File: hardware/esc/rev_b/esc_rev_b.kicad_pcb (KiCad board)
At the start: 6 copper layers, 150 x 150 mm, 646 parts, among them J1101 FUSED_BATTERY_TAP, J1102 MOTOR_PHASES, J1103 LOCAL_SWD, J1201 FUSED_BATTERY_TAP, J1202 MOTOR_PHASES, J1203 LOCAL_SWD, J1301 FUSED_BATTERY_TAP, J1302 MOTOR_PHASES, J1303 LOCAL_SWD, J1401 FUSED_BATTERY_TAP, J1402 MOTOR_PHASES, J1403 LOCAL_SWD, J1501 FUSED_BATTERY_TAP, J1502 MOTOR_PHASES, J1503 LOCAL_SWD, J1601 FUSED_BATTERY_TAP, J1602 MOTOR_PHASES, J1603 LOCAL_SWD, J201 ESC_SWD, J701 AUX_BATTERY, J702 FLIGHT_CAN_POWER, Q1101 IPTC014N10NM5, Q1102 IPTC014N10NM5, Q1103 IPTC014N10NM5, Q1104 IPTC014N10NM5, Q1105 IPTC014N10NM5, Q1106 IPTC014N10NM5, Q1201 IPTC014N10NM5, Q1202 IPTC014N10NM5, Q1203 IPTC014N10NM5, Q1204 IPTC014N10NM5, Q1205 IPTC014N10NM5, Q1206 IPTC014N10NM5, Q1301 IPTC014N10NM5, Q1302 IPTC014N10NM5, Q1303 IPTC014N10NM5, Q1304 IPTC014N10NM5, Q1305 IPTC014N10NM5, Q1306 IPTC014N10NM5, Q1401 IPTC014N10NM5, Q1402 IPTC014N10NM5, Q1403 IPTC014N10NM5, Q1404 IPTC014N10NM5, Q1405 IPTC014N10NM5, Q1406 IPTC014N10NM5, Q1501 IPTC014N10NM5, Q1502 IPTC014N10NM5, Q1503 IPTC014N10NM5, Q1504 IPTC014N10NM5, Q1505 IPTC014N10NM5, Q1506 IPTC014N10NM5, Q1601 IPTC014N10NM5, Q1602 IPTC014N10NM5, Q1603 IPTC014N10NM5, Q1604 IPTC014N10NM5, Q1605 IPTC014N10NM5, Q1606 IPTC014N10NM5, U1101 DRV8353SRTAR, U1102 STM32G431CBT6, U1103 ISO6731FDWR, U1104 TPS70933DBVR, U1105 INA296A2IDR, U1106 SN74LVC1G08DBVR, U1201 DRV8353SRTAR, U1202 STM32G431CBT6, U1203 ISO6731FDWR, U1204 TPS70933DBVR, U1205 INA296A2IDR, U1206 SN74LVC1G08DBVR, U1301 DRV8353SRTAR, U1302 STM32G431CBT6, U1303 ISO6731FDWR, U1304 TPS70933DBVR, U1305 INA296A2IDR, U1306 SN74LVC1G08DBVR, U1401 DRV8353SRTAR, U1402 STM32G431CBT6, U1403 ISO6731FDWR, U1404 TPS70933DBVR, U1405 INA296A2IDR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

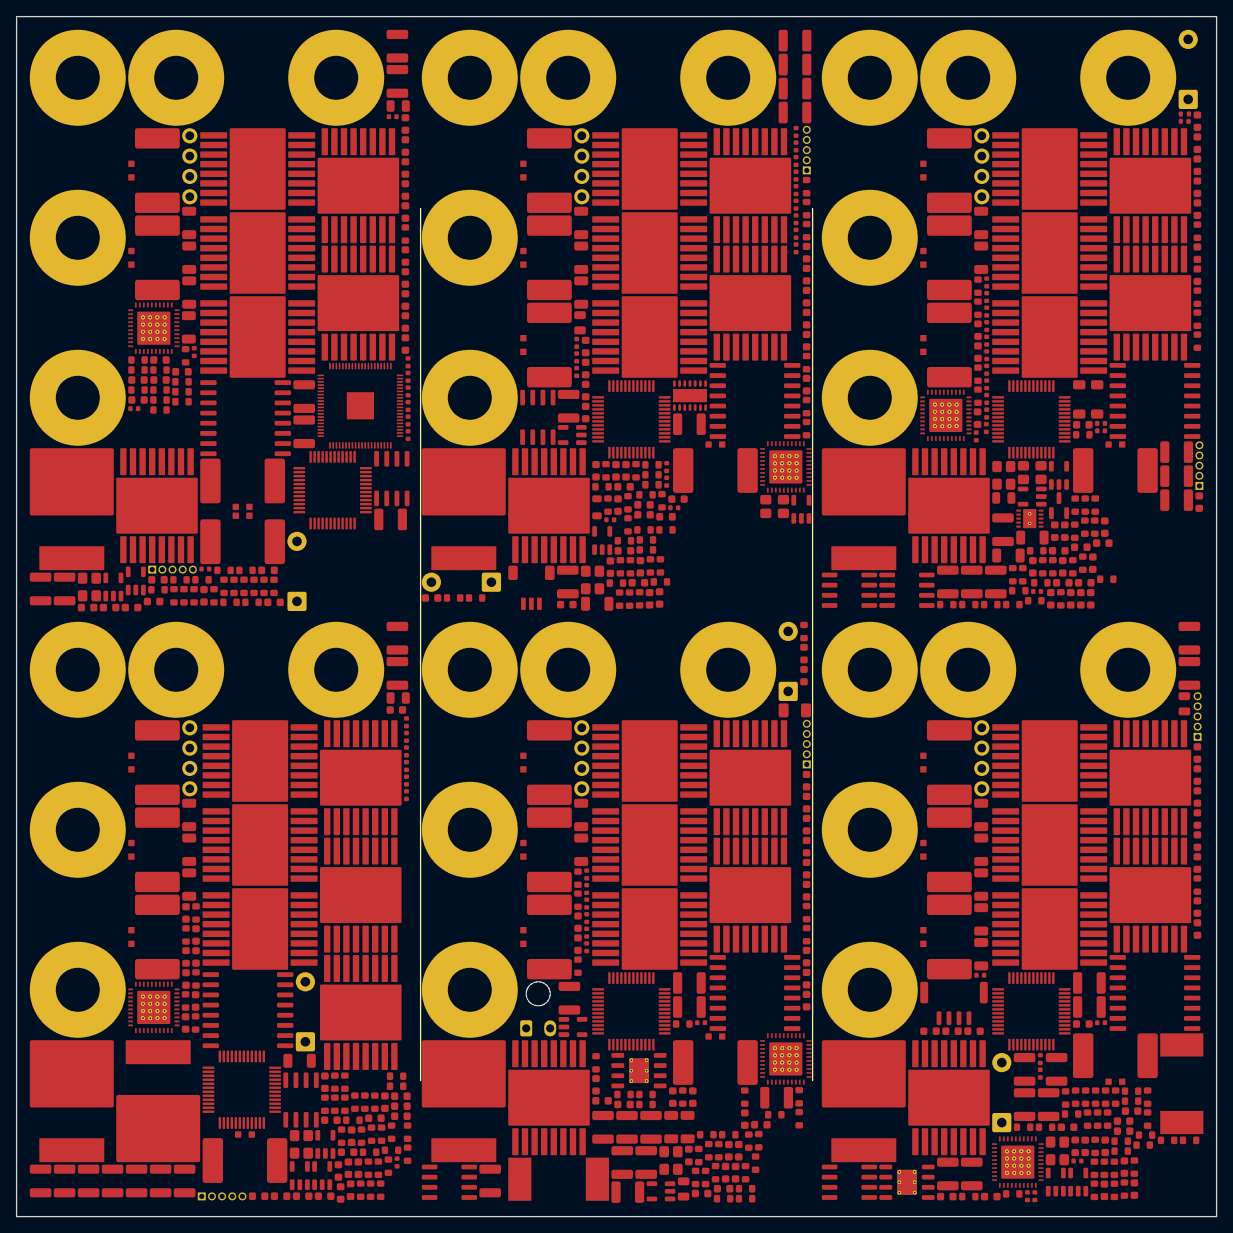
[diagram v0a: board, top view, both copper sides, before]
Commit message: esc: repack components without physical collisions
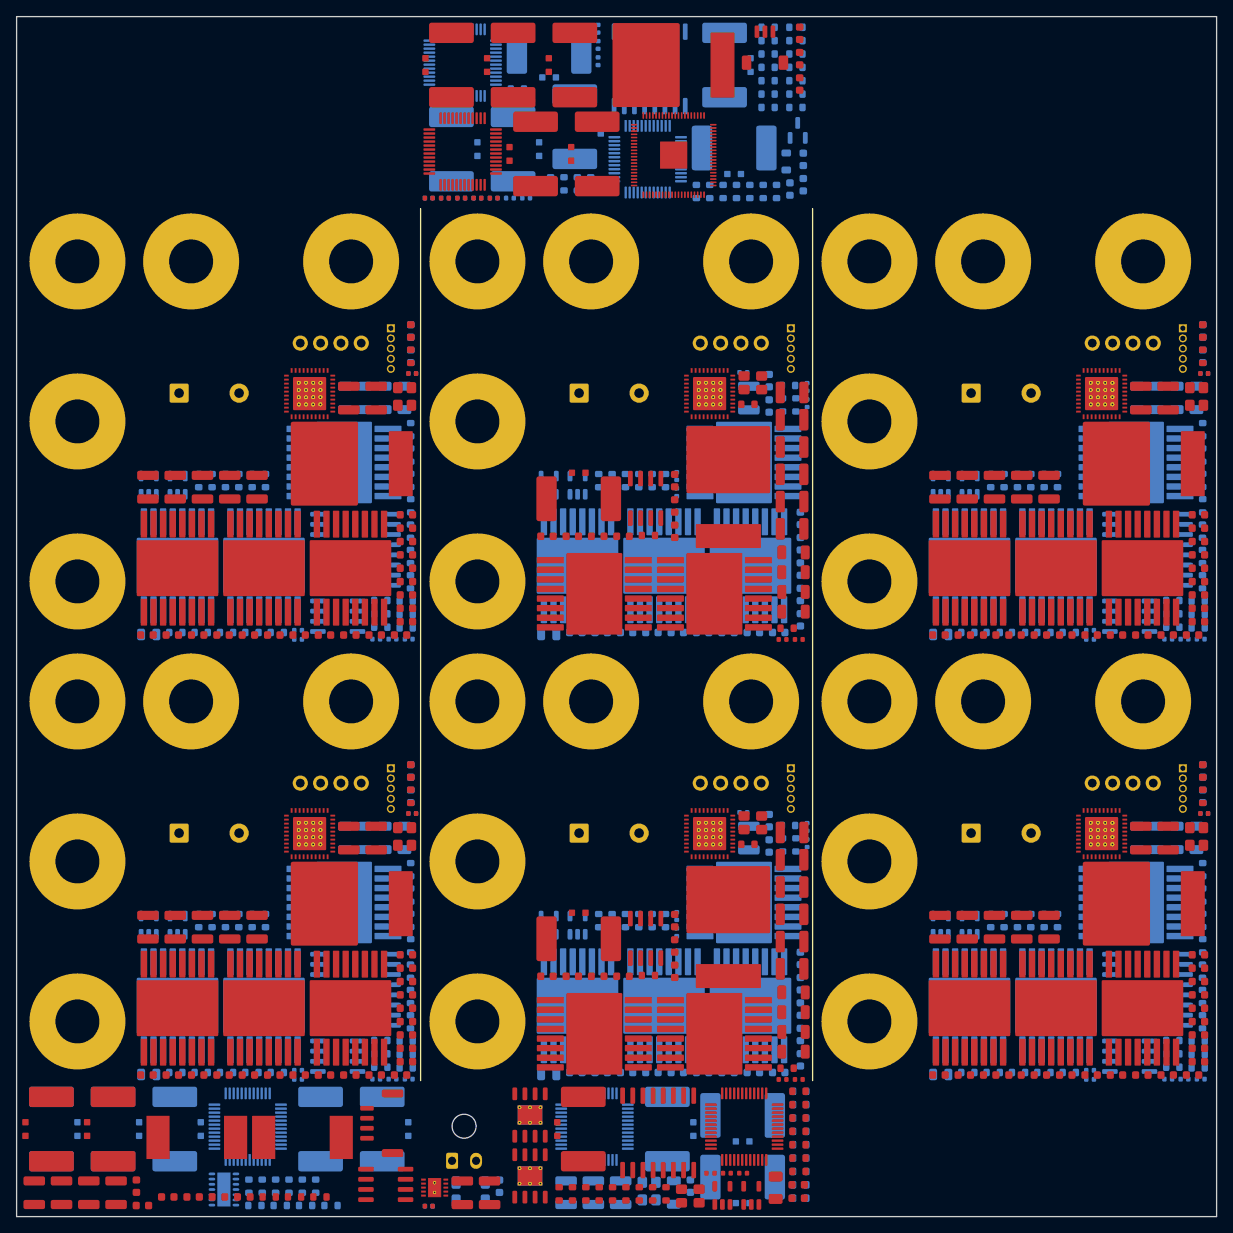
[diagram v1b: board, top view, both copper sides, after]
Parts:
- C1160, C1167, C1169, C1170, C1172, C1173, C1174, C1177, C1201, C1202, C1207, C1220, C1221, C1222, C1223, C1236, C1250, C1260, C1261, C1262, C1263, C1264, C1265, C1266, C1269, C1270, C1271, C1272, C1273, C1274, C1275, C1360, C1367, C1369, C1370, C1372, C1373, C1374, C1377, C1460, C1467, C1469, C1470, C1472, C1473, C1474, C1477, C1501, C1502, C1507, C1520, C1521, C1522, C1523, C1536, C1550, C1560, C1561, C1562, C1563, C1564, C1565, C1566, C1569, C1570, C1571, C1572, C1573, C1574, C1575, C1660, C1667, C1669, C1670, C1672, C1673, C1674, C1677, C201, C202, C205, C212, C213, C214, C215, C216, C217, C218, C219, C232, C233, C240, C241, C703, C706, C707, C711, C713, C714, D1102, D1302, D1402, D1602, D202, FL201, L201, Q1104, Q1105, Q1106, Q1203, Q1204, Q1205, Q1206, Q1304, Q1305, Q1306, Q1404, Q1405, Q1406, Q1503, Q1504, Q1505, Q1506, Q1604, Q1605, Q1606, R1102, R1103, R1104, R1105, R1106, R1107, R1108, R1109, R1110, R1111, R1112, R1120, R1121, R1122, R1123, R1130, R1131, R1132, R1133, R1140, R1141, R1142, R1143, R1144, R1145, R1150, R1151, R1152, R1153, R1154, R1155, R1156, R1157, R1158, R1159, R1204, R1205, R1206, R1207, R1208, R1209, R1210, R1211, R1212, R1221, R1222, R1230, R1231, R1232, R1233, R1244, R1245, R1250, R1251, R1252, R1253, R1254, R1255, R1256, R1257, R1258, R1259, R1302, R1303, R1304, R1305, R1306, R1307, R1308, R1309, R1310, R1311, R1312, R1330, R1331, R1332, R1333, R1340, R1341, R1342, R1343, R1344, R1345, R1350, R1351, R1352, R1353, R1354, R1355, R1356, R1357, R1358, R1359, R1402, R1403, R1404, R1405, R1406, R1407, R1408, R1409, R1410, R1411, R1412, R1420, R1421, R1422, R1430, R1431, R1432, R1433, R1440, R1441, R1442, R1443, R1444, R1445, R1450, R1451, R1452, R1453, R1454, R1455, R1456, R1457, R1458, R1459, R1504, R1505, R1506, R1507, R1508, R1509, R1510, R1511, R1512, R1521, R1522, R1523, R1530, R1531, R1532, R1533, R1544, R1602, R1603, R1604, R1605, R1606, R1607, R1608, R1609, R1610, R1611, R1612, R1620, R1621, R1630, R1631, R1632, R1633, R1640, R1641, R1642, R1643, R1644, R1645, R1650, R1651, R1652, R1653, R1654, R1655, R1656, R240, R241, R242, R701, R702, R703, R704, R705, R710, R711, R712, R713, TH1, TH2, TH3, TH4, U1102, U1103, U1104, U1105, U1106, U1202, U1203, U1204, U1206, U1303, U1304, U1305, U1306, U1402, U1403, U1404, U1405, U1406, U1504, U1506, U1602, U1603, U1604, U1605, U1606, U207, Y202: moved to B.Cu
- moved C231 147.2 mm to (15.7, 148.6), turned to 0 degrees
- moved C708 145.6 mm to (97.9, 2.08), turned to 90 degrees
- moved R201 145.1 mm to (86.7, 144.6)
- moved D701 144.8 mm to (81.8, 6.05), turned to 90 degrees
- moved C709 136.8 mm to (97.9, 5.25)
- moved C706 135.2 mm to (98.3, 17.8)
- moved D201 133.6 mm to (25.2, 147.5), turned to 0 degrees
- moved C712 133.6 mm to (97.9, 8.43)
- moved C205 133.3 mm to (51.5, 148.7), turned to 0 degrees
- moved FB201 132.1 mm to (28.4, 147.5), turned to 0 degrees
- moved R202 130.6 mm to (31.6, 147.5), turned to 0 degrees
- moved C702 127.3 mm to (2.21, 147.0)
- moved C707 126.0 mm to (98.3, 21.0)
- moved R1623 125.6 mm to (12.1, 139.1), turned to 90 degrees
- moved FL201 125.6 mm to (56.8, 146.9), turned to 0 degrees
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
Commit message: revert ESC to front-side-only placement from 325f93b; main board CANL routing + ACT45B pinout fix
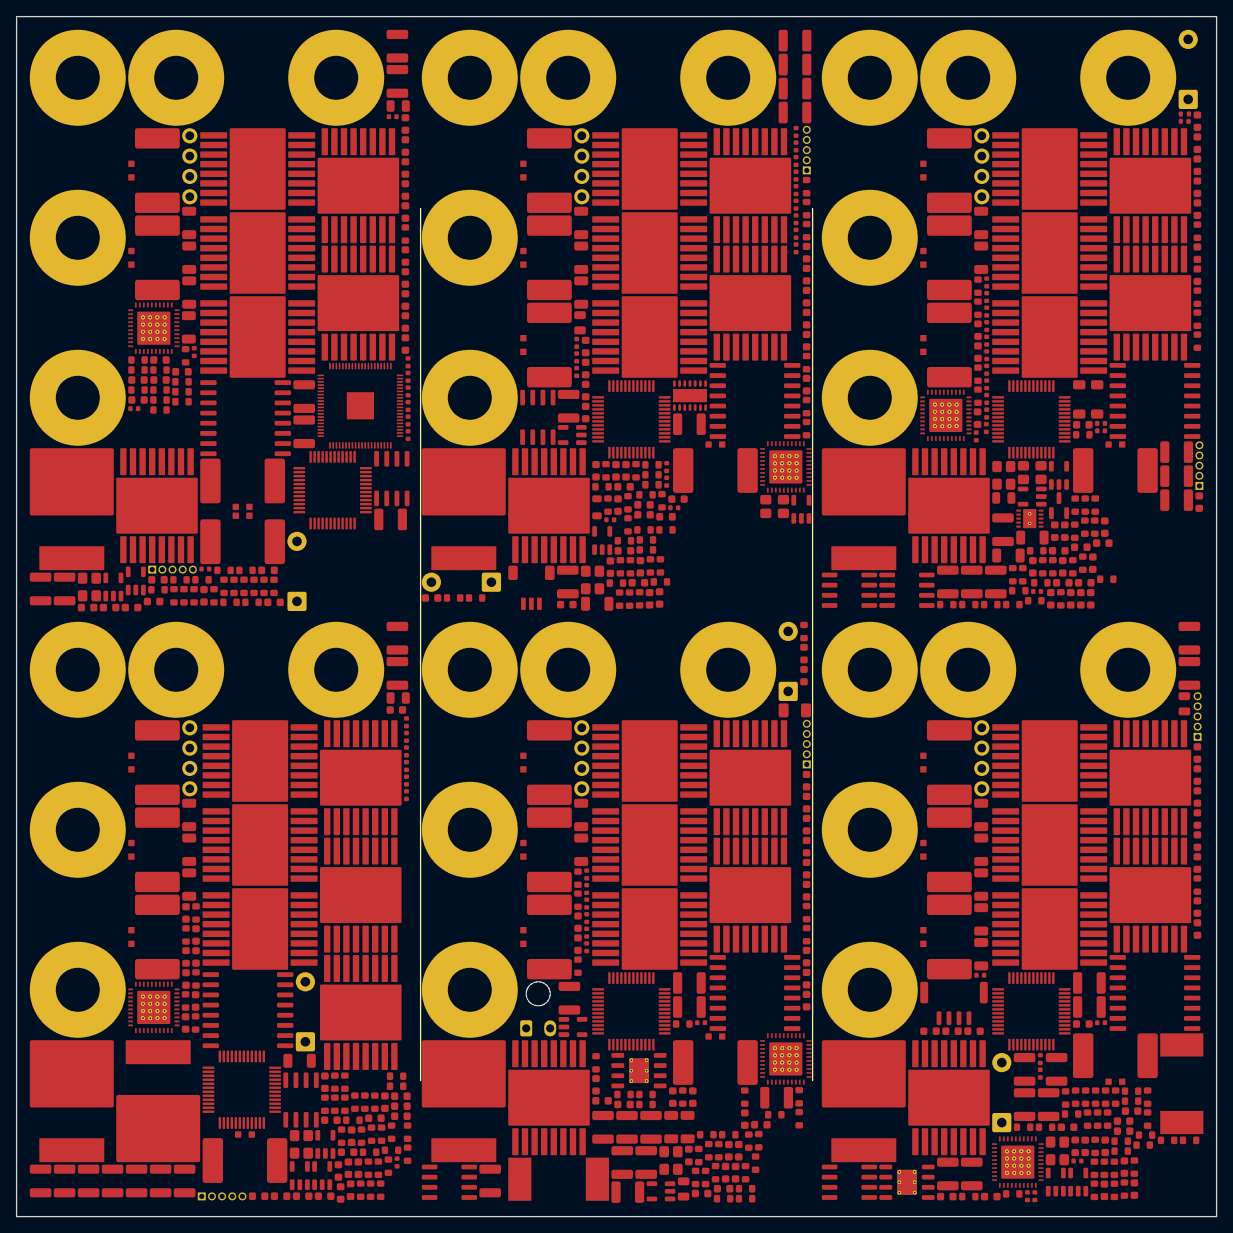
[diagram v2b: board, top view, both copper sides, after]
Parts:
- C1160, C1167, C1169, C1170, C1172, C1173, C1174, C1177, C1201, C1202, C1207, C1220, C1221, C1222, C1223, C1236, C1250, C1260, C1261, C1262, C1263, C1264, C1265, C1266, C1269, C1270, C1271, C1272, C1273, C1274, C1275, C1360, C1367, C1369, C1370, C1372, C1373, C1374, C1377, C1460, C1467, C1469, C1470, C1472, C1473, C1474, C1477, C1501, C1502, C1507, C1520, C1521, C1522, C1523, C1536, C1550, C1560, C1561, C1562, C1563, C1564, C1565, C1566, C1569, C1570, C1571, C1572, C1573, C1574, C1575, C1660, C1667, C1669, C1670, C1672, C1673, C1674, C1677, C201, C202, C205, C212, C213, C214, C215, C216, C217, C218, C219, C232, C233, C240, C241, C703, C706, C707, C711, C713, C714, D1102, D1302, D1402, D1602, D202, FL201, L201, Q1104, Q1105, Q1106, Q1203, Q1204, Q1205, Q1206, Q1304, Q1305, Q1306, Q1404, Q1405, Q1406, Q1503, Q1504, Q1505, Q1506, Q1604, Q1605, Q1606, R1102, R1103, R1104, R1105, R1106, R1107, R1108, R1109, R1110, R1111, R1112, R1120, R1121, R1122, R1123, R1130, R1131, R1132, R1133, R1140, R1141, R1142, R1143, R1144, R1145, R1150, R1151, R1152, R1153, R1154, R1155, R1156, R1157, R1158, R1159, R1204, R1205, R1206, R1207, R1208, R1209, R1210, R1211, R1212, R1221, R1222, R1230, R1231, R1232, R1233, R1244, R1245, R1250, R1251, R1252, R1253, R1254, R1255, R1256, R1257, R1258, R1259, R1302, R1303, R1304, R1305, R1306, R1307, R1308, R1309, R1310, R1311, R1312, R1330, R1331, R1332, R1333, R1340, R1341, R1342, R1343, R1344, R1345, R1350, R1351, R1352, R1353, R1354, R1355, R1356, R1357, R1358, R1359, R1402, R1403, R1404, R1405, R1406, R1407, R1408, R1409, R1410, R1411, R1412, R1420, R1421, R1422, R1430, R1431, R1432, R1433, R1440, R1441, R1442, R1443, R1444, R1445, R1450, R1451, R1452, R1453, R1454, R1455, R1456, R1457, R1458, R1459, R1504, R1505, R1506, R1507, R1508, R1509, R1510, R1511, R1512, R1521, R1522, R1523, R1530, R1531, R1532, R1533, R1544, R1602, R1603, R1604, R1605, R1606, R1607, R1608, R1609, R1610, R1611, R1612, R1620, R1621, R1630, R1631, R1632, R1633, R1640, R1641, R1642, R1643, R1644, R1645, R1650, R1651, R1652, R1653, R1654, R1655, R1656, R240, R241, R242, R701, R702, R703, R704, R705, R710, R711, R712, R713, TH1, TH2, TH3, TH4, U1102, U1103, U1104, U1105, U1106, U1202, U1203, U1204, U1206, U1303, U1304, U1305, U1306, U1402, U1403, U1404, U1405, U1406, U1504, U1506, U1602, U1603, U1604, U1605, U1606, U207, Y202: moved to F.Cu
- moved C231 147.2 mm to (136.0, 63.8), turned to 90 degrees
- moved C708 145.6 mm to (44.8, 137.7), turned to 180 degrees
- moved R201 145.1 mm to (146.0, 12.2)
- moved D701 144.8 mm to (17.7, 135.8), turned to 180 degrees
- moved C709 136.8 mm to (89.0, 141.8)
- moved C706 135.2 mm to (139.7, 146.6)
- moved D201 133.6 mm to (129.8, 64.3), turned to 90 degrees
- moved C712 133.6 mm to (90.3, 141.8)
- moved C205 133.3 mm to (97.4, 23.5), turned to 90 degrees
- moved FB201 132.1 mm to (131.0, 64.3), turned to 90 degrees
- moved R202 130.6 mm to (132.3, 64.3), turned to 90 degrees
- moved C702 127.3 mm to (129.0, 136.0)
- moved C707 126.0 mm to (46.0, 135.7)
- moved R1623 125.6 mm to (137.3, 129.9), turned to 180 degrees
- moved FL201 125.6 mm to (133.9, 47.9), turned to 90 degrees
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
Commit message: esc: restore physically valid all-front layout
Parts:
- moved J1301 214.9 mm to (12.0, 188.0), turned to 90 degrees
- moved PS1301 205.0 mm to (42.0, 208.0), turned to 0 degrees
- moved D1502 203.4 mm to (94.0, 283.0), turned to 0 degrees
- moved J1501 201.8 mm to (12.0, 272.0), turned to 90 degrees
- moved C1660 201.6 mm to (178.8, 284.9), turned to 0 degrees
- moved PS1501 201.3 mm to (42.0, 292.0), turned to 0 degrees
- moved C1330 200.8 mm to (13.0, 160.5), turned to 0 degrees
- moved PS1601 200.0 mm to (138.0, 292.0), turned to 0 degrees
- moved U1303 195.0 mm to (28.0, 206.0)
- moved C1504 194.8 mm to (45.4, 285.6)
- moved R1622 194.8 mm to (172.0, 280.0), turned to -90 degrees
- moved C1503 193.7 mm to (45.4, 281.8)
- moved C1571 193.2 mm to (93.3, 275.6)
- moved R1423 192.1 mm to (186.0, 207.4), turned to 0 degrees
- moved J1601 191.5 mm to (108.0, 272.0), turned to 90 degrees
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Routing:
- net /Motor 1 power cell/M1_SHC_N: track 0.00 -> 31.9 mm
- net /Motor 5 power cell/M5_SHC_N: track 0.00 -> 31.9 mm
- net /Motor 3 power cell/M3_SHC_N: track 0.00 -> 31.9 mm
- net /Motor 6 power cell/M6_SHC_N: track 0.00 -> 31.9 mm
- net /Motor 2 power cell/M2_SHC_N: track 0.00 -> 31.9 mm
- net /Motor 4 power cell/M4_SHC_N: track 0.00 -> 31.9 mm
- net /Motor 1 power cell/M1_SHC_P: track 0.00 -> 30.0 mm
- net /Motor 3 power cell/M3_SHC_P: track 0.00 -> 30.0 mm
- net /Motor 2 power cell/M2_SHC_P: track 0.00 -> 30.0 mm
- net /Motor 4 power cell/M4_SHC_P: track 0.00 -> 30.0 mm
- net /Motor 5 power cell/M5_SHC_P: track 0.00 -> 30.0 mm
- net /Motor 6 power cell/M6_SHC_P: track 0.00 -> 30.0 mm
- net /Motor 5 power cell/M5_SHA_N: track 0.00 -> 18.0 mm
- net /Motor 6 power cell/M6_SHA_N: track 0.00 -> 18.0 mm
- net /Motor 4 power cell/M4_SHA_N: track 0.00 -> 18.0 mm
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- added copper zone on B.Cu, net /DGND
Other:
- board size 150 x 150 mm -> 196 x 296 mm
- copper layers 6 -> 4
- board text added: "AUX POWER - TWO INDEPENDENT 1 A RAILS"
- board text added: "ESC SUPERVISOR / CAN FD"
- board text added: "MOTOR 1 - 60 A CELL"
- board text added: "MOTOR 2 - 60 A CELL"
- board text added: "MOTOR 3 - 60 A CELL"
- board text added: "MOTOR 4 - 60 A CELL"
- board text added: "MOTOR 5 - 60 A CELL"
- board text added: "MOTOR 6 - 60 A CELL"
- board text added: "REV-B | 4 oz OUTER / 1.5 oz INNER | 6 x 60 A"
- board text removed: "M1"
- board text removed: "M2"
- board text removed: "M3"
- board text removed: "M4"
- board text removed: "M5"
- board text removed: "M6"
- board text removed: "REV-B 150MM SIX-LAYER ESC PLACEMENT CANDIDATE"

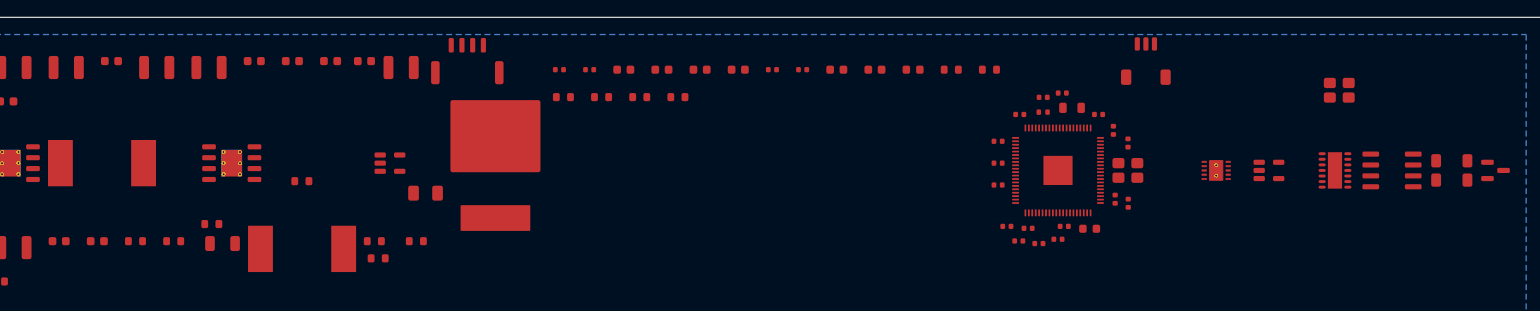
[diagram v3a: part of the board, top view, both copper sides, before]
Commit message: esc: hand route first ten signal links
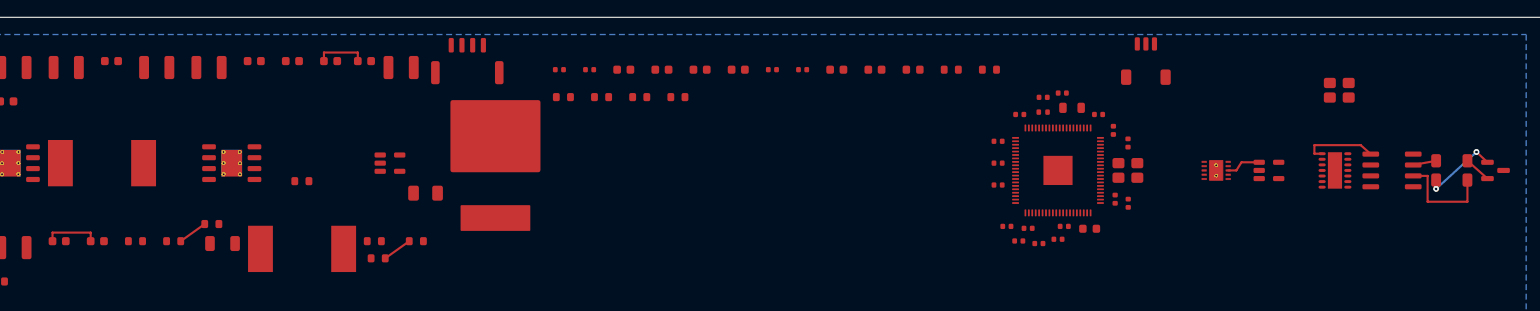
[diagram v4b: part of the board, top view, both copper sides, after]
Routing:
- net /Controller and ADC/U206_CANL: track 0.00 -> 11.9 mm
- net /CANH: track 0.00 -> 9.16 mm, vias 0 -> 2
- net /Controller and ADC/U207_TXCAN: track 0.00 -> 8.87 mm
- net /Auxiliary power/LM2_RIPPLE: track 0.00 -> 6.45 mm
- net /Auxiliary power/LM_RIPPLE: track 0.00 -> 5.95 mm
- net /Controller and ADC/ESC_RUN: track 0.00 -> 4.14 mm
- net /Auxiliary power/LM_FB: track 0.00 -> 3.44 mm
- net /Auxiliary power/LM2_FB: track 0.00 -> 3.44 mm
- net /CANL: track 0.00 -> 3.13 mm
- net /Controller and ADC/U206_CANH: track 0.00 -> 2.71 mm
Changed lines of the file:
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@@
 	)
 	(segment
+		(start 60.95 28.1)
+		(end 63.75 26.1)
+		(width 0.25)
+		(layer "F.Cu")
+		(net 9)
+	)
+	(segment
+		(start 22.15 25.1)
+		(end 26.6 25.1)
+		(width 0.25)
+		(layer "F.Cu")
+		(net 10)
+	)
+	(segment
+		(start 26.6 25.1)
+		(end 26.6 26.1)
+		(width 0.25)
+		(layer "F.Cu")
+		(net 10)
+	)
+	(segment
+		(start 22.15 26.1)
+		(end 22.15 25.1)
+		(width 0.25)
+		(layer "F.Cu")
+		(net 10)
+	)
+	(segment
+		(start 37.1 26.1)
+		(end 39.9 24.1)
+		(width 0.25)
+		(layer "F.Cu")
+		(net 14)
+	)
+	(segment
+		(start 53.8 4.099999)
+		(end 57.75 4.099999)
+		(width 0.25)
+		(layer "F.Cu")
+		(net 15)
+	)
+	(segment
+		(start 53.8 5.1)
+		(end 53.8 4.099999)
+		(width 0.25)
+		(layer "F.Cu")
+		(net 15)
+	)
+	(segment
+		(start 57.75 4.099999)
+		(end 57.75 5.1)
+		(width 0.25)
+		(layer "F.Cu")
+		(net 15)
+	)
+	(segment
+		(start 183.495 18.974999)
+		(end 183.495 20)
+		(width 0.25)
+		(layer "F.Cu")
+		(net 18)
+	)
+	(segment
+		(start 188.2 15.7)
+		(end 189.4825 16.899999)
+		(width 0.25)
+		(layer "F.Cu")
+		(net 18)
+	)
+	(via
+		(at 183.495 20)
+		(size 0.7)
+		(drill 0.3)
+		(layers "F.Cu" "B.Cu")
+		(net 18)
+	)
+	(via
+		(at 188.2 15.7)
+		(size 0.7)
+		(drill 0.3)
+		(layers "F.Cu" "B.Cu")
+		(net 18)
+	)
+	(segment
+		(start 183.495 20)
+		(end 188.2 15.7)
+		(width 0.25)
+		(layer "B.Cu")
+		(net 18)
+	)
+	(segment
+		(start 189.4825 18.799999)
+		(end 187.145 16.724999)
+		(width 0.25)
+		(layer "F.Cu")
+		(net 19)
+	)
+	(segment
+		(start 159.25 17.849999)
+		(end 160.2 17.85)
+		(width 0.25)
+		(layer "F.Cu")
+		(net 29)
+	)
+	(segment
+		(start 160.2 17.85)
+		(end 160.8 16.9)
+		(width 0.25)
+		(layer "F.Cu")
+		(net 29)
+	)
+	(segment
+		(start 160.8 16.9)
+		(end 162.8625 16.899999)
+		(width 0.25)
+		(layer "F.Cu")
+		(net 29)
+	)
+	(segment
+		(start 180.825 17.214999)
+		(end 183.495 16.724999)
+		(width 0.25)
+		(layer "F.Cu")
+		(net 35)
+	)
+	(segment
+		(start 182.5 21.5)
+		(end 187.145 21.5)
+		(width 0.25)
+		(layer "F.Cu")
+		(net 36)
+	)
+	(segment
+		(start 187.145 21.5)
+		(end 187.145 18.974999)
+		(width 0.25)
+		(layer "F.Cu")
+		(net 36)
+	)
+	(segment
+		(start 182.5 18.485)
+		(end 182.5 21.5)
+		(width 0.25)
+		(layer "F.Cu")
+		(net 36)
+	)
+	(segment
+		(start 180.825 18.484999)
+		(end 182.5 18.485)
+		(width 0.25)
+		(layer "F.Cu")
+		(net 36)
+	)
+	(segment
+		(start 169.3 14.9)
+		(end 174.7 14.9)
+		(width 0.25)
+		(layer "F.Cu")
+		(net 40)
+	)
+	(segment
+		(start 174.7 14.9)
+		(end 175.875 15.944999)
+		(width 0.25)
+		(layer "F.Cu")
+		(net 40)
+	)
+	(segment
+		(start 170.2 15.899999)
+		(end 169.3 15.9)
+		(width 0.25)
+		(layer "F.Cu")
+		(net 40)
+	)
+	(segment
+		(start 169.3 15.9)
+		(end 169.3 14.9)
+		(width 0.25)
+		(layer "F.Cu")
+		(net 40)
+	)
+	(segment
 		(start 87.1 113.6)
 		(end 84.85 111.35)
@@
 		(min_thickness 0.25)
 		(filled_areas_thickness no)
-		(fill
+		(fill yes
 			(thermal_gap 0.5)
 			(thermal_bridge_width 0.5)
